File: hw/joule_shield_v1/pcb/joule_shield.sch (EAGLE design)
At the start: 143 parts, among them J1 MF-CON-MICROUSB-RIGHT, J4 USB_AUSB_A_SMT_RA, J5 JST-ZH5SMT_RA, J6 INTEL_JOULE_J6, J7 INTEL_JOULE_J7, J8 DM3ATDM3AT, Q1 NFETEMT3F, Q2 NFETEMT3F, Q3 NFETEMT3F, Q4 NFETEMT3F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

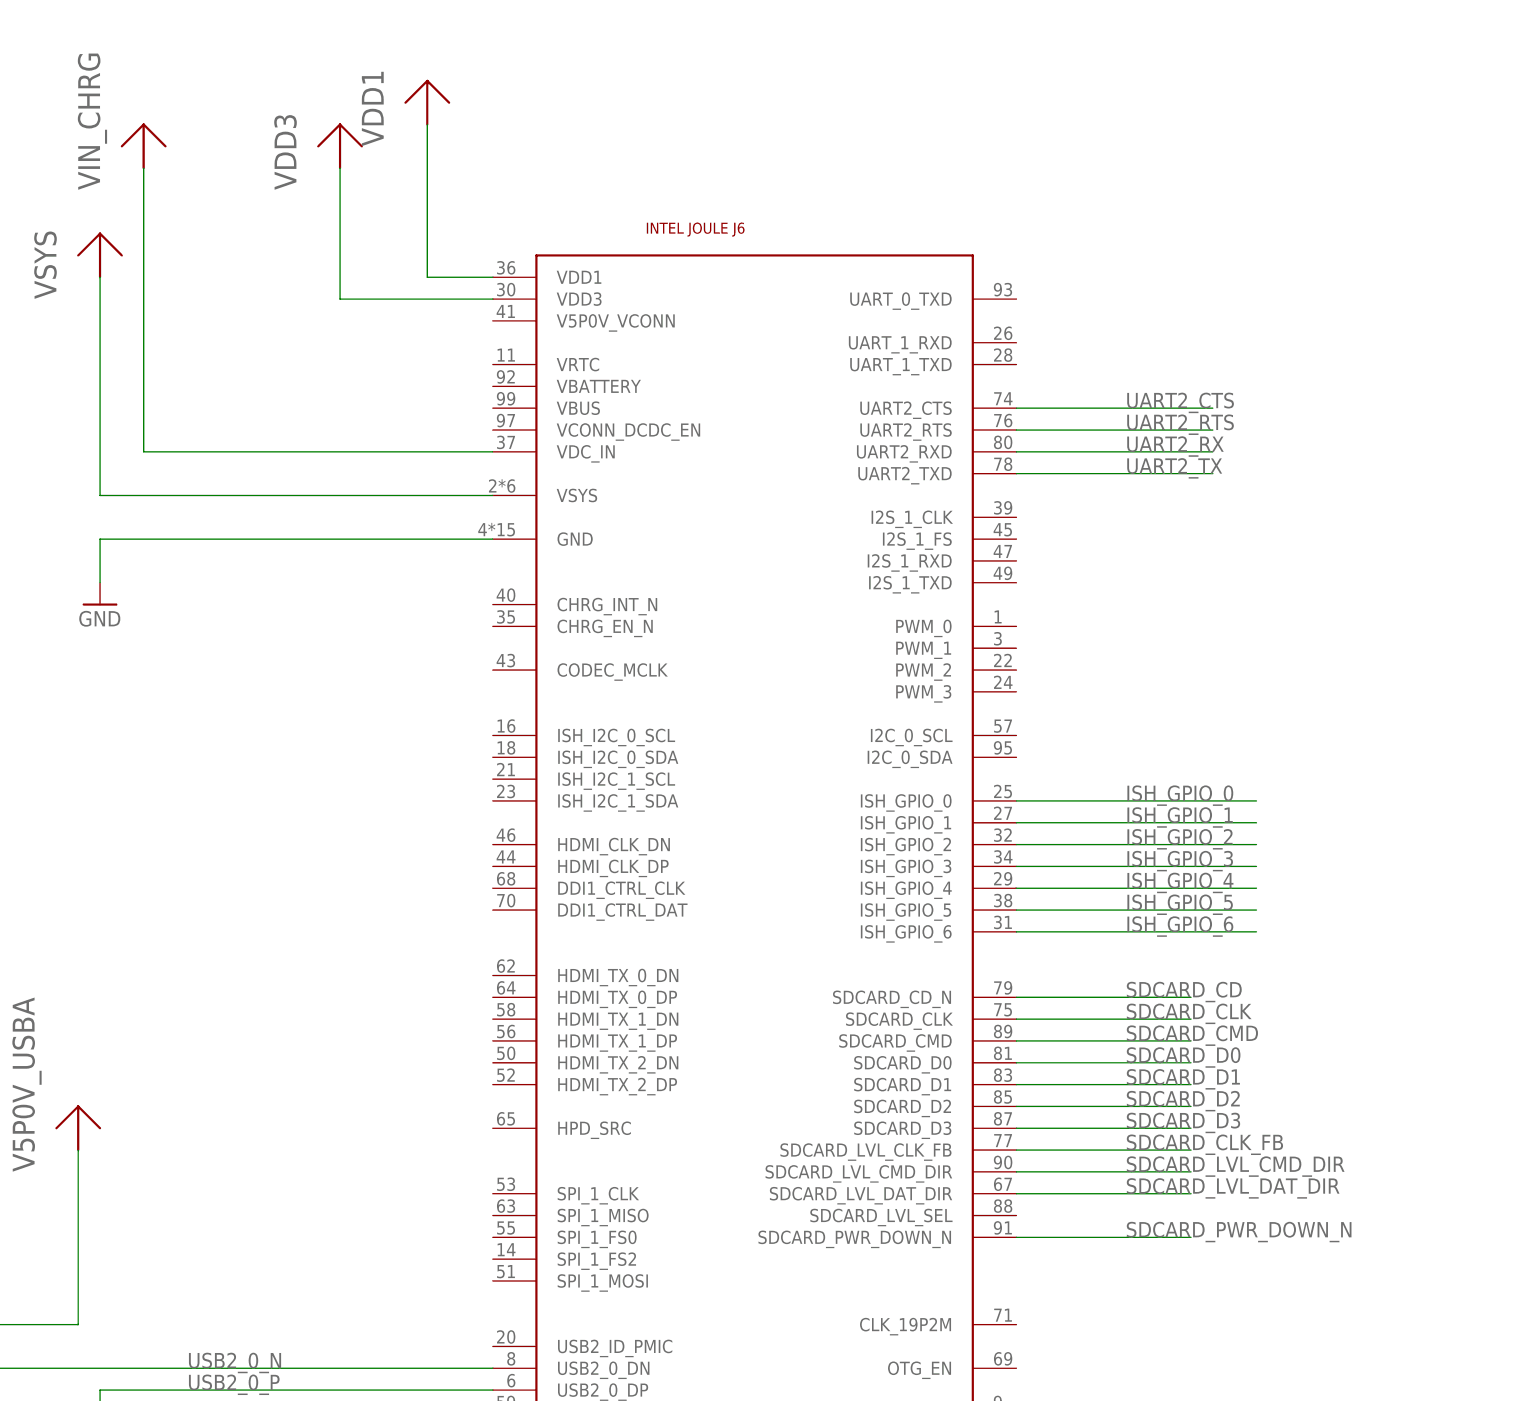
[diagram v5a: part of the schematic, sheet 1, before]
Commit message: joule shield: Run ERC and connect up some wires which were inadvertently left unconnected.
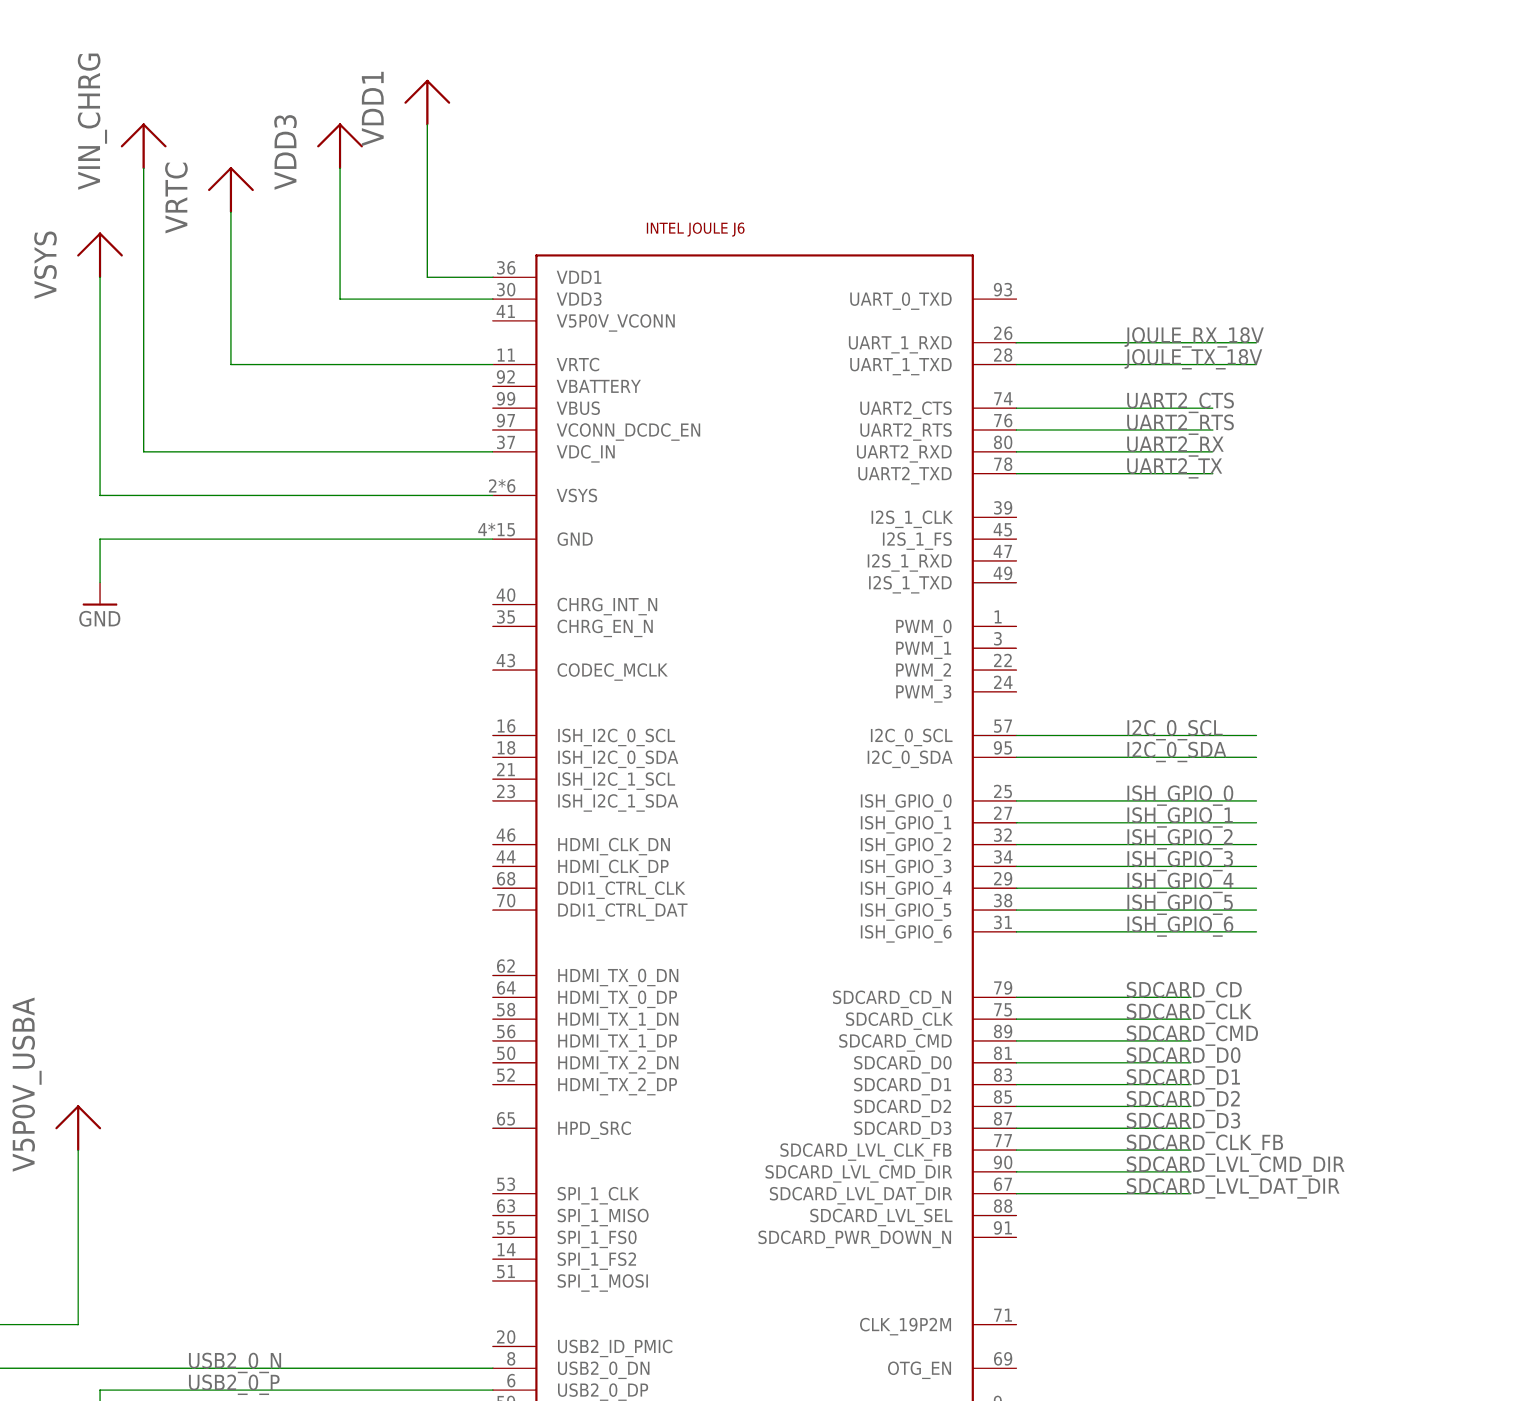
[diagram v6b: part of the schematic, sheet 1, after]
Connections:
- removed net SDCARD_PWR_DOWN_N: J6.SDCARD_PWR_DOWN_N
- net I2C_0_SCL: now also J6.I2C_0_SCL
- net I2C_0_SDA: now also J6.I2C_0_SDA
- net JOULE_RX_18V: now also J6.UART_1_RXD
- net JOULE_TX_18V: now also J6.UART_1_TXD
- net VRTC: now also J6.VRTC
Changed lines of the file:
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@@
 <part name="U$56" library="joule_shield" deviceset="VDD1" device=""/>
 <part name="U$57" library="joule_shield" deviceset="VDD1" device=""/>
+<part name="U$58" library="joule_shield" deviceset="VRTC" device=""/>
 </parts>
 <sheets>
@@
 <instance part="U$54" gate="G$1" x="104.14" y="-17.78"/>
 <instance part="U$55" gate="G$1" x="114.3" y="-17.78"/>
+<instance part="U$58" gate="G$1" x="-10.16" y="172.72"/>
 </instances>
 <busses>
@@
 </segment>
 </net>
-<net name="SDCARD_PWR_DOWN_N" class="0">
-<segment>
-<pinref part="J6" gate="G$1" pin="SDCARD_PWR_DOWN_N"/>
-<wire x1="81.28" y1="53.34" x2="101.6" y2="53.34" width="0.1524" layer="91"/>
-<label x="93.98" y="53.34" size="1.778" layer="95"/>
-</segment>
-</net>
 <net name="UART2_TX" class="0">
 <segment>
@@
 </segment>
 </net>
+<net name="JOULE_RX_18V" class="0">
+<segment>
+<pinref part="J6" gate="G$1" pin="UART_1_RXD"/>
+<wire x1="81.28" y1="157.48" x2="109.22" y2="157.48" width="0.1524" layer="91"/>
+<label x="93.98" y="157.48" size="1.778" layer="95"/>
+</segment>
+</net>
+<net name="JOULE_TX_18V" class="0">
+<segment>
+<pinref part="J6" gate="G$1" pin="UART_1_TXD"/>
+<wire x1="81.28" y1="154.94" x2="109.22" y2="154.94" width="0.1524" layer="91"/>
+<label x="93.98" y="154.94" size="1.778" layer="95"/>
+</segment>
+</net>
+<net name="VRTC" class="0">
+<segment>
+<pinref part="U$58" gate="G$1" pin="VRTC"/>
+<pinref part="J6" gate="G$1" pin="VRTC"/>
+<wire x1="20.32" y1="154.94" x2="-10.16" y2="154.94" width="0.1524" layer="91"/>
+<wire x1="-10.16" y1="154.94" x2="-10.16" y2="172.72" width="0.1524" layer="91"/>
+</segment>
+</net>
+<net name="I2C_0_SCL" class="0">
+<segment>
+<pinref part="J6" gate="G$1" pin="I2C_0_SCL"/>
+<wire x1="81.28" y1="111.76" x2="109.22" y2="111.76" width="0.1524" layer="91"/>
+<label x="93.98" y="111.76" size="1.778" layer="95"/>
+</segment>
+</net>
+<net name="I2C_0_SDA" class="0">
+<segment>
+<pinref part="J6" gate="G$1" pin="I2C_0_SDA"/>
+<wire x1="81.28" y1="109.22" x2="109.22" y2="109.22" width="0.1524" layer="91"/>
+<label x="93.98" y="109.22" size="1.778" layer="95"/>
+</segment>
+</net>

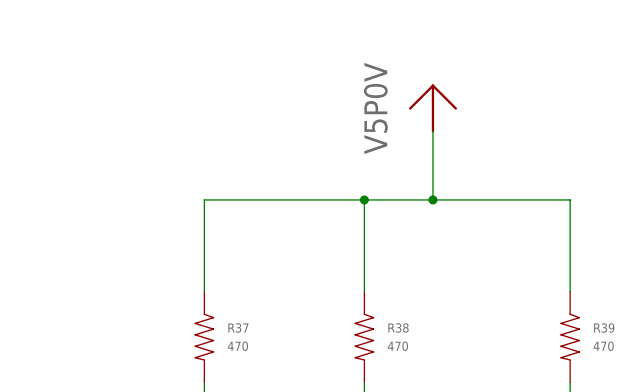
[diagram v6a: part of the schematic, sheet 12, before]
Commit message: joule shield: ground and power layout for FAN48623
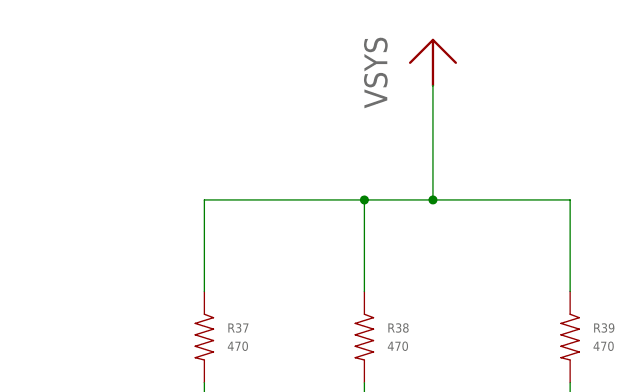
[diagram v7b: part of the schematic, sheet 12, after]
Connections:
- net V5P0V: no longer R12.P$1, R37.P$1, R38.P$1, R39.P$1
- net VSYS: now also R12.P$1, R37.P$1, R38.P$1, R39.P$1
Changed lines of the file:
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@@
 <part name="U$11" library="joule_shield" deviceset="VSYS" device=""/>
 <part name="U$12" library="joule_shield" deviceset="V5P0V" device=""/>
-<part name="U$13" library="joule_shield" deviceset="V5P0V" device=""/>
 <part name="U$14" library="joule_shield" deviceset="VSYS" device=""/>
 <part name="U$15" library="joule_shield" deviceset="VSYS" device=""/>
@@
 <attribute name="MPN" value="MF-RES-0603-470"/>
 </part>
-<part name="U$47" library="joule_shield" deviceset="V5P0V" device=""/>
 <part name="U$48" library="joule_shield" deviceset="SMTSO" device="SMTSO-M1.6"/>
 <part name="U$49" library="joule_shield" deviceset="SMTSO" device="SMTSO-M1.6"/>
@@
 <part name="U$57" library="joule_shield" deviceset="VDD1" device=""/>
 <part name="U$58" library="joule_shield" deviceset="VRTC" device=""/>
+<part name="U$47" library="joule_shield" deviceset="VSYS" device=""/>
+<part name="U$13" library="joule_shield" deviceset="VSYS" device=""/>
 </parts>
 <sheets>
@@
 <pinref part="U$11" gate="G$1" pin="VSYS"/>
 </segment>
+<segment>
+<pinref part="R12" gate="G$1" pin="P$1"/>
+<wire x1="127" y1="55.88" x2="127" y2="53.34" width="0.1524" layer="91"/>
+<pinref part="U$13" gate="G$1" pin="VSYS"/>
+</segment>
 </net>
 <net name="V5P0V" class="0">
@@
 <junction x="142.24" y="63.5"/>
 <pinref part="U$12" gate="G$1" pin="V5P0V"/>
-</segment>
-<segment>
-<pinref part="R12" gate="G$1" pin="P$1"/>
-<wire x1="127" y1="55.88" x2="127" y2="53.34" width="0.1524" layer="91"/>
-<pinref part="U$13" gate="G$1" pin="V5P0V"/>
 </segment>
 </net>
@@
 <instance part="R38" gate="G$1" x="68.58" y="63.5"/>
 <instance part="R39" gate="G$1" x="91.44" y="63.5"/>
-<instance part="U$47" gate="G$1" x="76.2" y="86.36"/>
 <instance part="Q1" gate="G$1" x="48.26" y="33.02">
 <attribute name="DPN" x="48.26" y="33.02" size="1.778" layer="96" display="off"/>
@@
 <attribute name="MPN" x="88.9" y="5.08" size="1.778" layer="96" display="off"/>
 </instance>
+<instance part="U$47" gate="G$1" x="76.2" y="91.44"/>
 </instances>
 <busses>
@@
 </segment>
 </net>
-<net name="V5P0V" class="0">
-<segment>
-<wire x1="76.2" y1="78.74" x2="76.2" y2="86.36" width="0.1524" layer="91"/>
-<pinref part="U$47" gate="G$1" pin="V5P0V"/>
+<net name="N$56" class="0">
+<segment>
+<pinref part="R39" gate="G$1" pin="P$2"/>
+<pinref part="D10" gate="G$1" pin="ANODE"/>
+<wire x1="91.44" y1="58.42" x2="91.44" y2="53.34" width="0.1524" layer="91"/>
+</segment>
+</net>
+<net name="N$57" class="0">
+<segment>
+<pinref part="R38" gate="G$1" pin="P$2"/>
+<pinref part="D9" gate="G$1" pin="ANODE"/>
+<wire x1="68.58" y1="58.42" x2="68.58" y2="53.34" width="0.1524" layer="91"/>
+</segment>
+</net>
+<net name="N$58" class="0">
+<segment>
+<pinref part="R37" gate="G$1" pin="P$2"/>
+<pinref part="D8" gate="G$1" pin="ANODE"/>
+<wire x1="50.8" y1="58.42" x2="50.8" y2="53.34" width="0.1524" layer="91"/>
+</segment>
+</net>
+<net name="N$59" class="0">
+<segment>
+<pinref part="D8" gate="G$1" pin="CATHODE"/>
+<wire x1="50.8" y1="48.26" x2="50.8" y2="40.64" width="0.1524" layer="91"/>
+<pinref part="Q1" gate="G$1" pin="D"/>
+</segment>
+</net>
+<net name="N$60" class="0">
+<segment>
+<pinref part="D9" gate="G$1" pin="CATHODE"/>
+<wire x1="68.58" y1="48.26" x2="68.58" y2="27.94" width="0.1524" layer="91"/>
+<pinref part="Q2" gate="G$1" pin="D"/>
+</segment>
+</net>
+<net name="N$61" class="0">
+<segment>
+<pinref part="D10" gate="G$1" pin="CATHODE"/>
+<wire x1="91.44" y1="48.26" x2="91.44" y2="12.7" width="0.1524" layer="91"/>
+<pinref part="Q3" gate="G$1" pin="D"/>
+</segment>
+</net>
+<net name="ISH_GPIO_0" class="0">
+<segment>
+<label x="7.62" y="33.02" size="1.778" layer="95"/>
+<pinref part="R33" gate="G$1" pin="P$2"/>
+<wire x1="38.1" y1="33.02" x2="43.18" y2="33.02" width="0.1524" layer="91"/>
+<pinref part="Q1" gate="G$1" pin="G"/>
+<wire x1="7.62" y1="33.02" x2="38.1" y2="33.02" width="0.1524" layer="91"/>
+<junction x="38.1" y="33.02"/>
+</segment>
+</net>
+<net name="ISH_GPIO_1" class="0">
+<segment>
+<wire x1="27.94" y1="20.32" x2="7.62" y2="20.32" width="0.1524" layer="91"/>
+<label x="7.62" y="20.32" size="1.778" layer="95"/>
+<pinref part="R34" gate="G$1" pin="P$2"/>
+<wire x1="27.94" y1="20.32" x2="60.96" y2="20.32" width="0.1524" layer="91"/>
+<pinref part="Q2" gate="G$1" pin="G"/>
+<junction x="27.94" y="20.32"/>
+</segment>
+</net>
+<net name="ISH_GPIO_2" class="0">
+<segment>
+<wire x1="33.02" y1="5.08" x2="7.62" y2="5.08" width="0.1524" layer="91"/>
+<label x="7.62" y="5.08" size="1.778" layer="95"/>
+<pinref part="R35" gate="G$1" pin="P$2"/>
+<wire x1="33.02" y1="5.08" x2="83.82" y2="5.08" width="0.1524" layer="91"/>
+<pinref part="Q3" gate="G$1" pin="G"/>
+<junction x="33.02" y="5.08"/>
+</segment>
+</net>
+<net name="VSYS" class="0">
+<segment>
+<pinref part="U$47" gate="G$1" pin="VSYS"/>
+<wire x1="76.2" y1="78.74" x2="76.2" y2="91.44" width="0.1524" layer="91"/>
 <wire x1="76.2" y1="78.74" x2="68.58" y2="78.74" width="0.1524" layer="91"/>
 <junction x="76.2" y="78.74"/>
@@
 </segment>
 </net>
-<net name="N$56" class="0">
-<segment>
-<pinref part="R39" gate="G$1" pin="P$2"/>
-<pinref part="D10" gate="G$1" pin="ANODE"/>
-<wire x1="91.44" y1="58.42" x2="91.44" y2="53.34" width="0.1524" layer="91"/>
-</segment>
-</net>
-<net name="N$57" class="0">
-<segment>
-<pinref part="R38" gate="G$1" pin="P$2"/>
-<pinref part="D9" gate="G$1" pin="ANODE"/>
-<wire x1="68.58" y1="58.42" x2="68.58" y2="53.34" width="0.1524" layer="91"/>
-</segment>
-</net>
-<net name="N$58" class="0">
-<segment>
-<pinref part="R37" gate="G$1" pin="P$2"/>
-<pinref part="D8" gate="G$1" pin="ANODE"/>
-<wire x1="50.8" y1="58.42" x2="50.8" y2="53.34" width="0.1524" layer="91"/>
-</segment>
-</net>
-<net name="N$59" class="0">
-<segment>
-<pinref part="D8" gate="G$1" pin="CATHODE"/>
-<wire x1="50.8" y1="48.26" x2="50.8" y2="40.64" width="0.1524" layer="91"/>
-<pinref part="Q1" gate="G$1" pin="D"/>
-</segment>
-</net>
-<net name="N$60" class="0">
-<segment>
-<pinref part="D9" gate="G$1" pin="CATHODE"/>
-<wire x1="68.58" y1="48.26" x2="68.58" y2="27.94" width="0.1524" layer="91"/>
-<pinref part="Q2" gate="G$1" pin="D"/>
-</segment>
-</net>
-<net name="N$61" class="0">
-<segment>
-<pinref part="D10" gate="G$1" pin="CATHODE"/>
-<wire x1="91.44" y1="48.26" x2="91.44" y2="12.7" width="0.1524" layer="91"/>
-<pinref part="Q3" gate="G$1" pin="D"/>
-</segment>
-</net>
-<net name="ISH_GPIO_0" class="0">
-<segment>
-<label x="7.62" y="33.02" size="1.778" layer="95"/>
-<pinref part="R33" gate="G$1" pin="P$2"/>
-<wire x1="38.1" y1="33.02" x2="43.18" y2="33.02" width="0.1524" layer="91"/>
-<pinref part="Q1" gate="G$1" pin="G"/>
-<wire x1="7.62" y1="33.02" x2="38.1" y2="33.02" width="0.1524" layer="91"/>
-<junction x="38.1" y="33.02"/>
-</segment>
-</net>
-<net name="ISH_GPIO_1" class="0">
-<segment>
-<wire x1="27.94" y1="20.32" x2="7.62" y2="20.32" width="0.1524" layer="91"/>
-<label x="7.62" y="20.32" size="1.778" layer="95"/>
-<pinref part="R34" gate="G$1" pin="P$2"/>
-<wire x1="27.94" y1="20.32" x2="60.96" y2="20.32" width="0.1524" layer="91"/>
-<pinref part="Q2" gate="G$1" pin="G"/>
-<junction x="27.94" y="20.32"/>
-</segment>
-</net>
-<net name="ISH_GPIO_2" class="0">
-<segment>
-<wire x1="33.02" y1="5.08" x2="7.62" y2="5.08" width="0.1524" layer="91"/>
-<label x="7.62" y="5.08" size="1.778" layer="95"/>
-<pinref part="R35" gate="G$1" pin="P$2"/>
-<wire x1="33.02" y1="5.08" x2="83.82" y2="5.08" width="0.1524" layer="91"/>
-<pinref part="Q3" gate="G$1" pin="G"/>
-<junction x="33.02" y="5.08"/>
-</segment>
-</net>
